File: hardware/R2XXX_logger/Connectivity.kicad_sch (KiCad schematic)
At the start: 1 part, among them J1 USB4500-03-0-A

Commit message: Throws flatbuf packets
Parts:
- added J2: A79618-001, CC_Connectors:OMNETICS_A79618-001, symbol CC_Connectors:A79618-001
- added J3: S2B-PH-K-S_LF, CC_Connectors:JST_S2B-PH-K-S_LF, symbol CC_Connectors:S2B-PH-K-S_LF
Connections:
- net GND: now reaches J1.A1 (GND)
- net GND: now also J1.A12 (GND), J1.B1 (GND), J1.B12 (GND)
- net +5V: now reaches J1.A4 (VBUS)
- net +5V: now also J1.A9 (VBUS), J1.B4 (VBUS), J1.B9 (VBUS)
- net USB_CC1: now reaches J1.A5 (CC1)
- net USB_DP: now reaches J1.A6 (DP1)
- net USB_DP: now also J1.B6 (DP2)
- net USB_DN: now reaches J1.A7 (DN1)
- net USB_DN: now also J1.B7 (DN2)
- net USB_CC2: now reaches J1.B5 (CC2)
- no-connect marks 0 -> 2
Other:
- moved on the sheet: J1

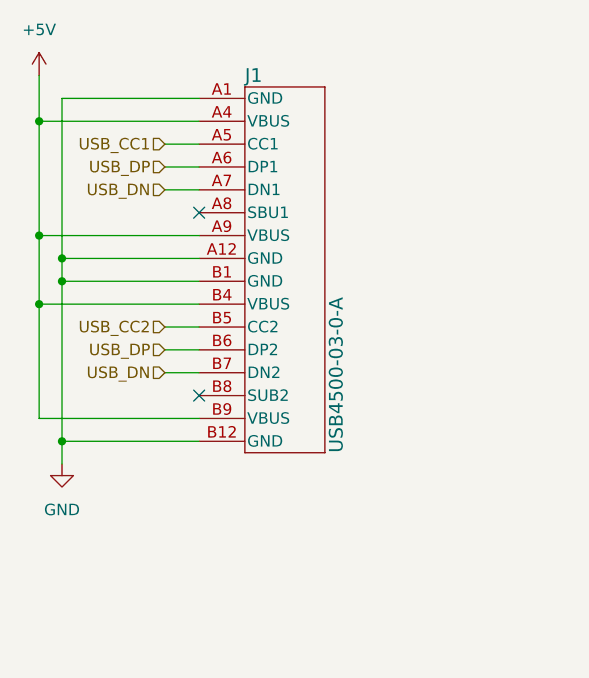
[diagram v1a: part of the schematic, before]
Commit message: Adding the flatbuffer stack causes it to crash
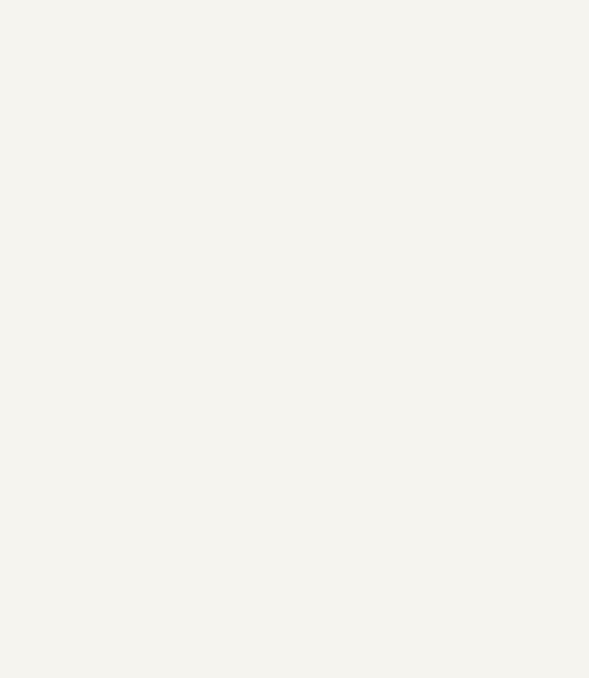
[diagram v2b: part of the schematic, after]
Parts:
- removed J1: USB4500-03-0-A, CC_Connectors:CONN_USB4500_GCT, symbol CC_Connectors:USB4500-03-0-A
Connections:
- no-connect marks 2 -> 0
